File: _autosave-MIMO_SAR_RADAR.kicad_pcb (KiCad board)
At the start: 2 copper layers, 43 parts, among them IC1 SKY13418-485LF, IC10 PSA2-6+, IC11 ADL5380ACPZ-R7, IC12 ADL5380ACPZ-R7, IC13 ADL5380ACPZ-R7, IC14 ADL5380ACPZ-R7, IC15 SKY13418-485LF, IC16 ADA4940-2ACPZ-RL, IC17 ADA4940-2ACPZ-RL, IC18 ADA4940-2ACPZ-RL, IC19 ADA4940-2ACPZ-RL, IC2 SKY13418-485LF, IC20 ADS8588SIPM, IC21 LMX2594RHAT, IC22 SKY13418-485LF, IC23 SKY13418-485LF, IC3 SKY13418-485LF, IC4 SKY13418-485LF, IC5 LMX2572RHAT, IC5 LT3042IMSE#PBF, IC6 PMA3-73-1W+, IC7 PSA2-6+, IC8 PSA2-6+, IC9 PSA2-6+, U1 MAX5035AUSA, U2 STM32H7A3IGTx, U3 ESP32-C3-WROOM-02, U4 TSR2-24120, Y1 SiT9121AI-2B1-33E100.000000G

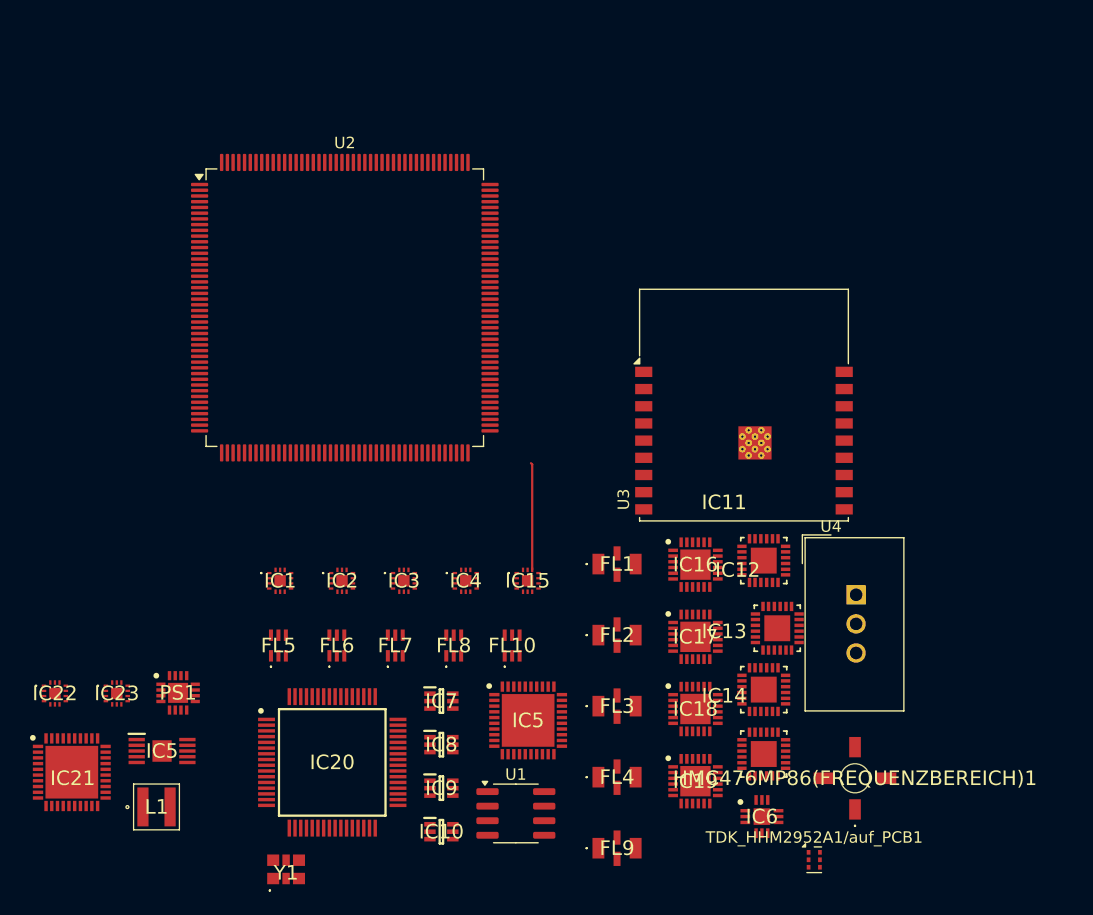
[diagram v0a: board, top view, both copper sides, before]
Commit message: Structure +2.nd rx channel
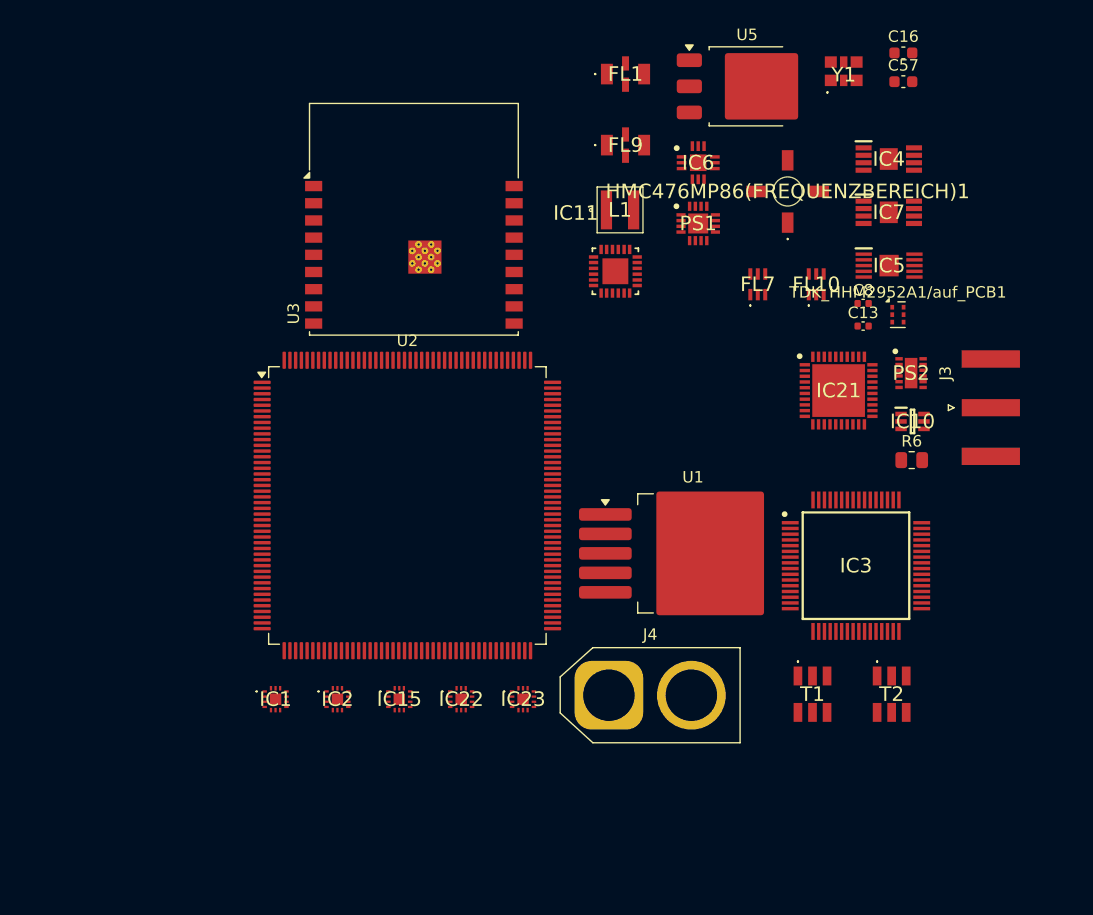
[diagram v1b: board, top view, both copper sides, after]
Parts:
- removed FL2, FL3, FL4: LFCN-6000+, RF_LP:LFCN6000
- removed FL5, FL6, FL8: HFCG-3000+, RF_HP:HFCG3000
- removed IC12, IC13, IC14: ADL5380ACPZ-R7, RF_Modulators:QFN50P400X400X100-25N
- removed IC16, IC17, IC18, IC19: ADA4940-2ACPZ-RL, ADC_DRIVER:QFN50P400X400X80-25N-D
- removed IC20: ADS8588SIPM, HS_ADC:QFP50P1200X1200X160-64N
- removed the IC5 at (34.0, 86.1)
- removed the IC5 at (66.0, 83.5)
- removed IC8, IC9: PSA2-6+, LNA:SOT65P215X100-6N
- removed U4: TSR2-24120, Converter_DCDC:Converter_DCDC_TRACO_TSR2-xxxx_THT
- added C13: 100pF, Capacitor_SMD:C_0402_1005Metric, F.Cu at (95.2, 49.0)
- added C16: 0.1uF, Capacitor_SMD:C_0603_1608Metric, F.Cu at (98.8, 25.2)
- added C57: 0.01uF, Capacitor_SMD:C_0603_1608Metric, F.Cu at (98.8, 27.7)
- added C8: 100pF, Capacitor_SMD:C_0402_1005Metric, F.Cu at (95.2, 47.1)
- added IC5: LT3042IMSE#PBF, Low_noise_LDO:SOP50P490X110-11N, F.Cu at (97.5, 43.8)
- added J3: Conn_Coaxial_Small, Connector_Coaxial:SMA_Amphenol_132289_EdgeMount, F.Cu at (106.4, 56.2)
- added J4: Conn_01x02_Pin, Connector_AMASS:AMASS_XT60-M_1x02_P7.20mm_Vertical, F.Cu at (73.0, 81.2)
- added PS2: LM27762DSSR, LM27762DSSR:SON50P200X300X80-13N-D, F.Cu at (99.4, 53.1)
- added R6: 93.1R, Resistor_SMD:R_0805_2012Metric, F.Cu at (99.5, 60.7)
- added T1: TCM1-63AX-2+, Balun:TCM163AX2, F.Cu at (90.8, 81.2)
- added T2: TCM1-63AX-2+, Balun:TCM163AX2, F.Cu at (97.7, 81.2)
- added U5: LM1117DT-3.3, Package_TO_SOT_SMD:TO-252-3_TabPin2, F.Cu at (85.1, 28.1)
- IC3: value SKY13418-485LF -> ADS8584SIPM; footprint SKY13:SKY13418485LF -> 4CH_ADC:QFP50P1200X1200X160-64N
- IC4: value SKY13418-485LF -> OPA1632DGNR; footprint SKY13:SKY13418485LF -> DIFF_AMPS:SOP65P490X110-9N
- IC7: value PSA2-6+ -> OPA1632DGNR; footprint LNA:SOT65P215X100-6N -> DIFF_AMPS:SOP65P490X110-9N
- U1: value MAX5035AUSA -> LM2596S-12; footprint Package_SO:SOIC-8_3.9x4.9mm_P1.27mm -> Package_TO_SOT_SMD:TO-263-5_TabPin3
- moved Y1 85.0 mm to (93.5, 26.8)
- moved IC21 74.8 mm to (93.1, 54.7)
- moved L1 66.0 mm to (74.0, 38.9)
- moved FL9 61.4 mm to (74.5, 33.2)
- moved PS1 61.1 mm to (80.8, 40.1)
- moved IC7 57.8 mm to (97.5, 39.1)
- moved IC6 57.3 mm to (80.8, 34.8)
- moved IC10 54.5 mm to (99.5, 57.4)
- moved IC4 52.1 mm to (97.5, 34.5)
- moved HMC476MP86(FREQUENZBEREICH)1 51.6 mm to (88.7, 37.3)
- moved TDK_HHM2952A1/auf_PCB1 48.1 mm to (98.3, 48.0)
- moved FL7 44.7 mm to (86.0, 45.4)
- moved FL1 42.8 mm to (74.5, 27.0)
- moved FL10 41.2 mm to (91.1, 45.4)
- moved IC3 39.5 mm to (94.6, 69.9)
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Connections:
- FL1 pad 1: unconnected-(FL1-RF_IN-Pad1) -> Net-(FL1-RF_IN)
- FL1 pad 3: unconnected-(FL1-RF_OUT-Pad3) -> Net-(FL1-RF_OUT)
- FL1 pad 4: unconnected-(FL1-GROUND_2-Pad4) -> GND
- FL7 pad 1: unconnected-(FL7-INPUT-Pad1) -> Net-(FL1-RF_OUT)
- FL7 pad 3: unconnected-(FL7-OUTPUT-Pad3) -> Net-(FL7-OUTPUT)
- IC1 pad 13: unconnected-(IC1-ANT-Pad13) -> Net-(FL1-RF_IN)
- IC1 pad 15: unconnected-(IC1-GND-Pad15) -> GND
- IC1 pad 4: unconnected-(IC1-VDD-Pad4) -> +3.3V
- IC1 pad 5: unconnected-(IC1-V3-Pad5) -> RX1_B2
- IC1 pad 6: unconnected-(IC1-V2-Pad6) -> RX1_B1
- IC1 pad 7: unconnected-(IC1-V1-Pad7) -> RX1_B0
- IC10 pad 1: unconnected-(IC10-RF-IN-Pad1) -> Net-(IC10-RF-IN)
- IC10 pad 2: unconnected-(IC10-GND_1-Pad2) -> GND
- IC10 pad 3: unconnected-(IC10-GND_2-Pad3) -> GND
- IC10 pad 4: unconnected-(IC10-RF-OUT_&_VD-Pad4) -> Net-(IC10-RF-OUT_&_VD)
- IC10 pad 5: unconnected-(IC10-GND_3-Pad5) -> GND
- IC10 pad 6: unconnected-(IC10-GND_4-Pad6) -> GND
- IC11 pad 1: unconnected-(IC11-GND3_2-Pad1) -> GND
- IC11 pad 10: unconnected-(IC11-LOIN-Pad10) -> Net-(IC11-LOIN)
- IC11 pad 11: unconnected-(IC11-GND4-Pad11) -> GND
- IC11 pad 13: unconnected-(IC11-VCC2-Pad13) -> 5V_CLEAN
- IC11 pad 14: unconnected-(IC11-GND2_2-Pad14) -> GND
- IC11 pad 15: unconnected-(IC11-QLO-Pad15) -> Net-(IC11-QLO)
- IC11 pad 16: unconnected-(IC11-QHI-Pad16) -> Net-(IC11-QHI)
- IC11 pad 17: unconnected-(IC11-GND2-Pad17) -> GND
- IC11 pad 18: unconnected-(IC11-GND3_3-Pad18) -> GND
- IC11 pad 19: unconnected-(IC11-ADJ-Pad19) -> Net-(IC11-ADJ)
- IC11 pad 2: unconnected-(IC11-GND1_2-Pad2) -> GND
- IC11 pad 20: unconnected-(IC11-GND3_4-Pad20) -> GND
- IC11 pad 21: unconnected-(IC11-REFIN-Pad21) -> Net-(IC11-REFIN)
- IC11 pad 22: unconnected-(IC11-REFIP-Pad22) -> Net-(IC11-REFIP)
- IC11 pad 23: unconnected-(IC11-GND3-Pad23) -> GND
- IC11 pad 24: unconnected-(IC11-VDD3-Pad24) -> 5V_CLEAN
- IC11 pad 3: unconnected-(IC11-IHI-Pad3) -> IHI1
- IC11 pad 4: unconnected-(IC11-ILO-Pad4) -> ILO1
- IC11 pad 5: unconnected-(IC11-GND1-Pad5) -> GND
- IC11 pad 6: unconnected-(IC11-VCC1-Pad6) -> 5V_CLEAN
- IC11 pad 7: unconnected-(IC11-ENBL-Pad7) -> Net-(IC11-ENBL)
- IC11 pad 8: unconnected-(IC11-GND4_2-Pad8) -> GND
- IC11 pad 9: unconnected-(IC11-LOIP-Pad9) -> Net-(IC11-LOIP)
- IC15 pad 4: unconnected-(IC15-VDD-Pad4) -> +3.3V
- IC2 pad 15: unconnected-(IC2-GND-Pad15) -> GND
- IC2 pad 4: unconnected-(IC2-VDD-Pad4) -> +3.3V
- IC2 pad 5: unconnected-(IC2-V3-Pad5) -> RX2_B2
- IC2 pad 6: unconnected-(IC2-V2-Pad6) -> RX2_B1
- IC2 pad 7: unconnected-(IC2-V1-Pad7) -> RX2_B0
- IC21 pad 23: Net-(HMC476MP86(FREQUENZBEREICH)1-RF_IN) -> Net-(IC21-RFOUTAP)
- IC22 pad 4: unconnected-(IC22-VDD-Pad4) -> +3.3V
- IC23 pad 13: unconnected-(IC23-ANT-Pad13) -> Net-(IC23-ANT)
- IC23 pad 4: unconnected-(IC23-VDD-Pad4) -> +3.3V
- IC23 pad 6: unconnected-(IC23-V2-Pad6) -> Net-(IC23-V2)
- IC23 pad 7: unconnected-(IC23-V1-Pad7) -> Net-(IC23-V1)
- IC4 pad 1: unconnected-(IC4-RF5-Pad1) -> Net-(IC4-VIN-)
- IC4 pad 2: unconnected-(IC4-RF3-Pad2) -> GND
- IC4 pad 7: unconnected-(IC4-V1-Pad7) -> Net-(IC4-ENABLE)
- IC4 pad 8: unconnected-(IC4-N/C-Pad8) -> Net-(IC4-VIN+)
- IC4 pad 9: unconnected-(IC4-RF2-Pad9) -> GND
- IC6 pad 2: Net-(HMC476MP86(FREQUENZBEREICH)1-RF-OUT_AND_DC-IN) -> Net-(IC6-RF-IN)
- IC7 pad 1: unconnected-(IC7-RF-IN-Pad1) -> Net-(IC7-VIN-)
- IC7 pad 2: unconnected-(IC7-GND_1-Pad2) -> GND
- TDK_HHM2952A1/auf_PCB1 pad 2: unconnected-(TDK_HHM2952A1/auf_PCB1-Coupled-Pad2) -> SPLIT_TX
- TDK_HHM2952A1/auf_PCB1 pad 5: unconnected-(TDK_HHM2952A1/auf_PCB1-Isolated-Pad5) -> Net-(TDK_HHM2952A1/auf_PCB1-Isolated)
- TDK_HHM2952A1/auf_PCB1 pad 6: unconnected-(TDK_HHM2952A1/auf_PCB1-Direct-Pad6) -> Net-(J3-In)
- U1 pad 1: unconnected-(U1-BST-Pad1) -> Net-(D3-K)
- U1 pad 2: unconnected-(U1-VD-Pad2) -> Net-(D2-K)
- U1 pad 3: unconnected-(U1-SGND-Pad3) -> GND
- U1 pad 4: unconnected-(U1-FB-Pad4) -> Net-(U1-FB)
- U1 pad 5: unconnected-(U1-ON/~{OFF}-Pad5) -> GND
- U2 pad 102: Net-(U2-VSS-Pad102) -> GND
- U2 pad 103: unconnected-(U2-VDD-Pad103) -> +3.3V
- U2 pad 113: Net-(U2-VSS-Pad102) -> GND
- U2 pad 126: Net-(U2-VSS-Pad102) -> GND
- U2 pad 127: unconnected-(U2-VDD-Pad127) -> +3.3V
- U2 pad 135: Net-(U2-VSS-Pad102) -> GND
- U2 pad 136: unconnected-(U2-VDD-Pad136) -> +3.3V
- U2 pad 14: Net-(U2-VSS-Pad102) -> GND
- U2 pad 148: Net-(U2-VSS-Pad102) -> GND
- U2 pad 15: unconnected-(U2-VDD-Pad15) -> +3.3V
- U2 pad 158: Net-(U2-VSS-Pad102) -> GND
- U2 pad 159: unconnected-(U2-VDD-Pad159) -> +3.3V
- U2 pad 172: unconnected-(U2-VDD-Pad172) -> +3.3V
- U2 pad 22: Net-(U2-VSS-Pad102) -> GND
- U2 pad 23: unconnected-(U2-VDD-Pad23) -> +3.3V
- U2 pad 36: unconnected-(U2-VDD-Pad36) -> +3.3V
- U2 pad 37: unconnected-(U2-VSSA-Pad37) -> GND
- U2 pad 48: Net-(U2-VSS-Pad102) -> GND
- U2 pad 49: unconnected-(U2-VDD-Pad49) -> +3.3V
- U2 pad 61: Net-(U2-VSS-Pad102) -> GND
- U2 pad 62: unconnected-(U2-VDD-Pad62) -> +3.3V
- U2 pad 71: Net-(U2-VSS-Pad102) -> GND
- U2 pad 72: unconnected-(U2-VDD-Pad72) -> +3.3V
- U2 pad 82: unconnected-(U2-VDD-Pad82) -> +3.3V
- U2 pad 90: Net-(U2-VSS-Pad102) -> GND
- U2 pad 91: unconnected-(U2-VDD-Pad91) -> +3.3V
- U3 pad 19: Net-(U3-GND-Pad19) -> GND
- U3 pad 9: Net-(U3-GND-Pad19) -> GND
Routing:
- net unconnected-(IC15-RF8-Pad12): track 9.35 -> 0.00 mm
